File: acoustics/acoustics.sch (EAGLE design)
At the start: 174 parts

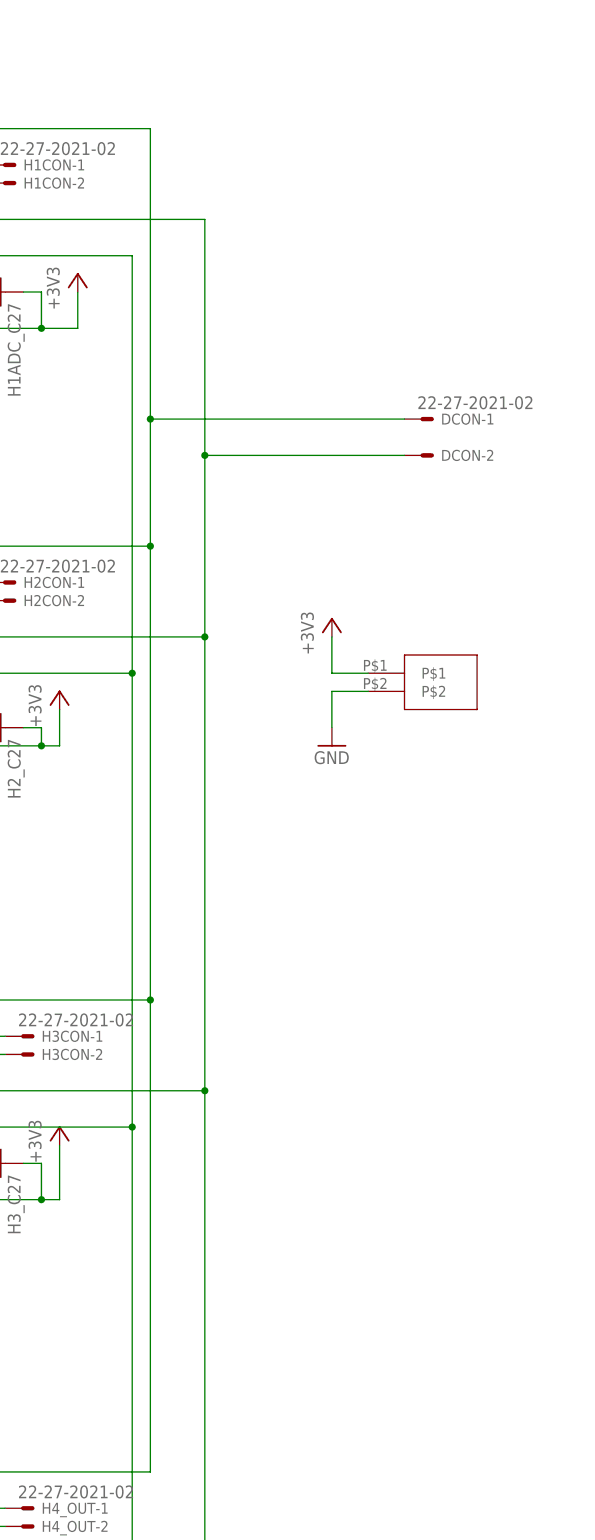
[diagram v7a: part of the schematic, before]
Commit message: Adding connectors and labels
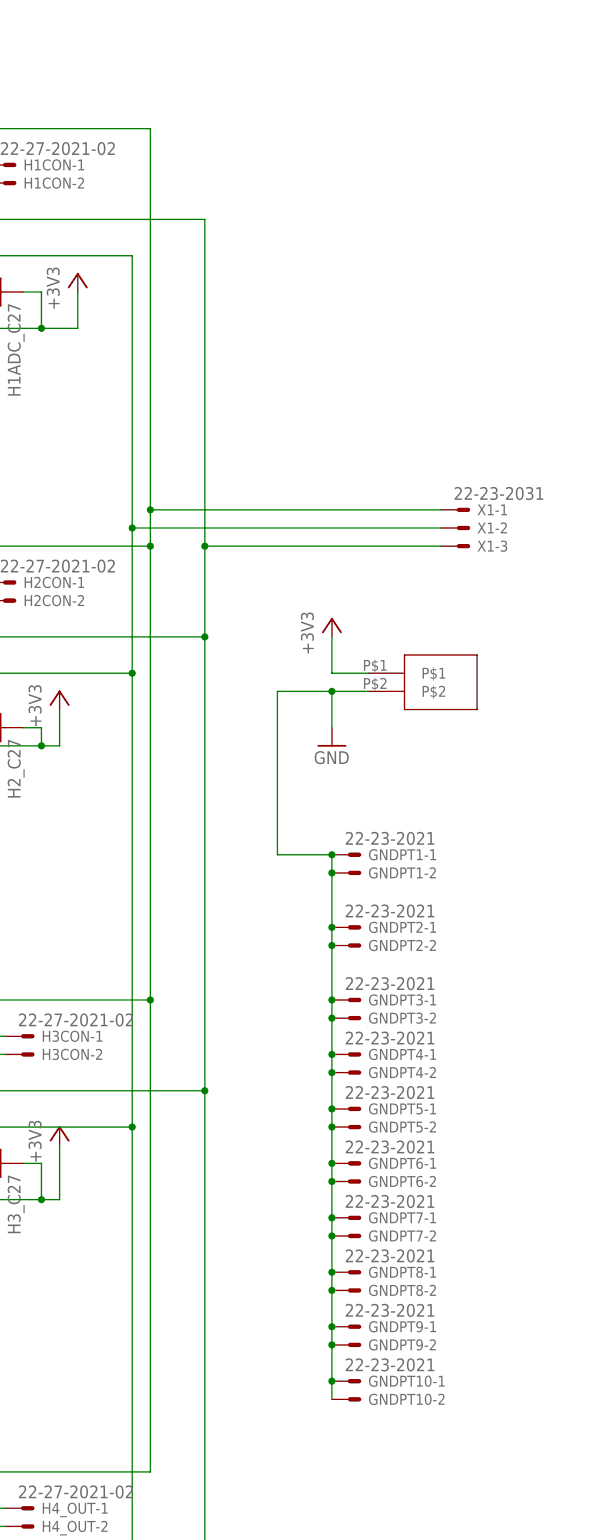
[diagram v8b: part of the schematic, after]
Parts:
- removed DCON: 22-27-2021-02, con-molex:22-27-2021-02
- added GNDPT1, GNDPT10, GNDPT2, GNDPT3, GNDPT4, GNDPT5, GNDPT6, GNDPT7, GNDPT8, GNDPT9: 22-23-2021, con-molex:22-23-2021
- added X1: 22-23-2031, con-molex:22-23-2031
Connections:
- net CLK: now also X1-2.S
- net GND: now also GNDPT1-1.S, GNDPT1-2.S, GNDPT10-1.S, GNDPT10-2.S, GNDPT2-1.S, GNDPT2-2.S, GNDPT3-1.S, GNDPT3-2.S, GNDPT4-1.S, GNDPT4-2.S, GNDPT5-1.S, GNDPT5-2.S, GNDPT6-1.S, GNDPT6-2.S, GNDPT7-1.S, GNDPT7-2.S, GNDPT8-1.S, GNDPT8-2.S, GNDPT9-1.S, GNDPT9-2.S
- net SCLK: now also X1-3.S; no longer DCON-2.S
- net START: now also X1-1.S; no longer DCON-1.S
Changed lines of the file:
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@@
 <part name="H3RF_C6" library="rcl" library_urn="urn:adsk.eagle:library:334" deviceset="C-EU" device="C0603" package3d_urn="urn:adsk.eagle:package:23616/2" value="47uf"/>
 <part name="H4_DIFAMP" library="THS4551" deviceset="THS4551" device=""/>
-<part name="DCON" library="con-molex" library_urn="urn:adsk.eagle:library:165" deviceset="22-?-02" device="27-2021"/>
 <part name="+3V21" library="supply1" library_urn="urn:adsk.eagle:library:371" deviceset="+3V3" device=""/>
 <part name="GND5" library="supply1" library_urn="urn:adsk.eagle:library:371" deviceset="GND" device=""/>
 <part name="U$2" library="105313-1102" deviceset="105313-1102" device=""/>
+<part name="X1" library="con-molex" library_urn="urn:adsk.eagle:library:165" deviceset="22-23-2031" device=""/>
+<part name="GNDPT1" library="con-molex" library_urn="urn:adsk.eagle:library:165" deviceset="22-23-2021" device=""/>
+<part name="GNDPT2" library="con-molex" library_urn="urn:adsk.eagle:library:165" deviceset="22-23-2021" device=""/>
+<part name="GNDPT3" library="con-molex" library_urn="urn:adsk.eagle:library:165" deviceset="22-23-2021" device=""/>
+<part name="GNDPT4" library="con-molex" library_urn="urn:adsk.eagle:library:165" deviceset="22-23-2021" device=""/>
+<part name="GNDPT5" library="con-molex" library_urn="urn:adsk.eagle:library:165" deviceset="22-23-2021" device=""/>
+<part name="GNDPT6" library="con-molex" library_urn="urn:adsk.eagle:library:165" deviceset="22-23-2021" device=""/>
+<part name="GNDPT7" library="con-molex" library_urn="urn:adsk.eagle:library:165" deviceset="22-23-2021" device=""/>
+<part name="GNDPT8" library="con-molex" library_urn="urn:adsk.eagle:library:165" deviceset="22-23-2021" device=""/>
+<part name="GNDPT9" library="con-molex" library_urn="urn:adsk.eagle:library:165" deviceset="22-23-2021" device=""/>
+<part name="GNDPT10" library="con-molex" library_urn="urn:adsk.eagle:library:165" deviceset="22-23-2021" device=""/>
 </parts>
 <sheets>
@@
 <instance part="H3RF_C6" gate="G$1" x="144.78" y="-73.66" rot="R180"/>
 <instance part="H4_DIFAMP" gate="G$1" x="30.48" y="-119.38"/>
-<instance part="DCON" gate="-1" x="337.82" y="33.02"/>
-<instance part="DCON" gate="-2" x="337.82" y="27.94"/>
 <instance part="+3V21" gate="G$1" x="325.12" y="5.08"/>
 <instance part="GND5" gate="1" x="325.12" y="-12.7"/>
 <instance part="U$2" gate="G$1" x="335.28" y="-5.08"/>
+<instance part="X1" gate="-1" x="342.9" y="20.32"/>
+<instance part="X1" gate="-2" x="342.9" y="17.78"/>
+<instance part="X1" gate="-3" x="342.9" y="15.24"/>
+<instance part="GNDPT1" gate="-1" x="327.66" y="-27.94"/>
+<instance part="GNDPT1" gate="-2" x="327.66" y="-30.48"/>
+<instance part="GNDPT2" gate="-1" x="327.66" y="-38.1"/>
+<instance part="GNDPT2" gate="-2" x="327.66" y="-40.64"/>
+<instance part="GNDPT3" gate="-1" x="327.66" y="-48.26"/>
+<instance part="GNDPT3" gate="-2" x="327.66" y="-50.8"/>
+<instance part="GNDPT4" gate="-1" x="327.66" y="-55.88"/>
+<instance part="GNDPT4" gate="-2" x="327.66" y="-58.42"/>
+<instance part="GNDPT5" gate="-1" x="327.66" y="-63.5"/>
+<instance part="GNDPT5" gate="-2" x="327.66" y="-66.04"/>
+<instance part="GNDPT6" gate="-1" x="327.66" y="-71.12"/>
+<instance part="GNDPT6" gate="-2" x="327.66" y="-73.66"/>
+<instance part="GNDPT7" gate="-1" x="327.66" y="-78.74"/>
+<instance part="GNDPT7" gate="-2" x="327.66" y="-81.28"/>
+<instance part="GNDPT8" gate="-1" x="327.66" y="-86.36"/>
+<instance part="GNDPT8" gate="-2" x="327.66" y="-88.9"/>
+<instance part="GNDPT9" gate="-1" x="327.66" y="-93.98"/>
+<instance part="GNDPT9" gate="-2" x="327.66" y="-96.52"/>
+<instance part="GNDPT10" gate="-1" x="327.66" y="-101.6"/>
+<instance part="GNDPT10" gate="-2" x="327.66" y="-104.14"/>
 </instances>
 <busses>
@@
 <pinref part="ADC_H1" gate="G$1" pin="START"/>
 <wire x1="236.22" y1="73.66" x2="299.72" y2="73.66" width="0.1524" layer="91"/>
-<wire x1="299.72" y1="73.66" x2="299.72" y2="33.02" width="0.1524" layer="91"/>
+<wire x1="299.72" y1="73.66" x2="299.72" y2="20.32" width="0.1524" layer="91"/>
 <junction x="299.72" y="15.24"/>
-<pinref part="DCON" gate="-1" pin="S"/>
-<wire x1="299.72" y1="33.02" x2="299.72" y2="15.24" width="0.1524" layer="91"/>
-<wire x1="335.28" y1="33.02" x2="299.72" y2="33.02" width="0.1524" layer="91"/>
-<junction x="299.72" y="33.02"/>
+<pinref part="X1" gate="-1" pin="S"/>
+<wire x1="299.72" y1="20.32" x2="299.72" y2="15.24" width="0.1524" layer="91"/>
+<wire x1="340.36" y1="20.32" x2="299.72" y2="20.32" width="0.1524" layer="91"/>
+<junction x="299.72" y="20.32"/>
 </segment>
 </net>
@@
 <wire x1="325.12" y1="-5.08" x2="325.12" y2="-10.16" width="0.1524" layer="91"/>
 <pinref part="U$2" gate="G$1" pin="P$2"/>
+<pinref part="GNDPT10" gate="-2" pin="S"/>
+<pinref part="GNDPT10" gate="-1" pin="S"/>
+<wire x1="325.12" y1="-104.14" x2="325.12" y2="-101.6" width="0.1524" layer="91"/>
+<pinref part="GNDPT9" gate="-2" pin="S"/>
+<wire x1="325.12" y1="-101.6" x2="325.12" y2="-96.52" width="0.1524" layer="91"/>
+<junction x="325.12" y="-101.6"/>
+<pinref part="GNDPT9" gate="-1" pin="S"/>
+<wire x1="325.12" y1="-96.52" x2="325.12" y2="-93.98" width="0.1524" layer="91"/>
+<junction x="325.12" y="-96.52"/>
+<pinref part="GNDPT8" gate="-2" pin="S"/>
+<wire x1="325.12" y1="-93.98" x2="325.12" y2="-88.9" width="0.1524" layer="91"/>
+<junction x="325.12" y="-93.98"/>
+<pinref part="GNDPT8" gate="-1" pin="S"/>
+<wire x1="325.12" y1="-88.9" x2="325.12" y2="-86.36" width="0.1524" layer="91"/>
+<junction x="325.12" y="-88.9"/>
+<pinref part="GNDPT7" gate="-2" pin="S"/>
+<wire x1="325.12" y1="-86.36" x2="325.12" y2="-81.28" width="0.1524" layer="91"/>
+<junction x="325.12" y="-86.36"/>
+<pinref part="GNDPT7" gate="-1" pin="S"/>
+<wire x1="325.12" y1="-81.28" x2="325.12" y2="-78.74" width="0.1524" layer="91"/>
+<junction x="325.12" y="-81.28"/>
+<pinref part="GNDPT6" gate="-2" pin="S"/>
+<wire x1="325.12" y1="-78.74" x2="325.12" y2="-73.66" width="0.1524" layer="91"/>
+<junction x="325.12" y="-78.74"/>
+<pinref part="GNDPT6" gate="-1" pin="S"/>
+<wire x1="325.12" y1="-73.66" x2="325.12" y2="-71.12" width="0.1524" layer="91"/>
+<junction x="325.12" y="-73.66"/>
+<pinref part="GNDPT5" gate="-2" pin="S"/>
+<wire x1="325.12" y1="-71.12" x2="325.12" y2="-66.04" width="0.1524" layer="91"/>
+<junction x="325.12" y="-71.12"/>
+<pinref part="GNDPT5" gate="-1" pin="S"/>
+<wire x1="325.12" y1="-66.04" x2="325.12" y2="-63.5" width="0.1524" layer="91"/>
+<junction x="325.12" y="-66.04"/>
+<pinref part="GNDPT4" gate="-2" pin="S"/>
+<wire x1="325.12" y1="-63.5" x2="325.12" y2="-58.42" width="0.1524" layer="91"/>
+<junction x="325.12" y="-63.5"/>
+<pinref part="GNDPT4" gate="-1" pin="S"/>
+<wire x1="325.12" y1="-58.42" x2="325.12" y2="-55.88" width="0.1524" layer="91"/>
+<junction x="325.12" y="-58.42"/>
+<pinref part="GNDPT3" gate="-2" pin="S"/>
+<wire x1="325.12" y1="-55.88" x2="325.12" y2="-50.8" width="0.1524" layer="91"/>
+<junction x="325.12" y="-55.88"/>
+<pinref part="GNDPT3" gate="-1" pin="S"/>
+<wire x1="325.12" y1="-50.8" x2="325.12" y2="-48.26" width="0.1524" layer="91"/>
+<junction x="325.12" y="-50.8"/>
+<pinref part="GNDPT2" gate="-2" pin="S"/>
+<wire x1="325.12" y1="-48.26" x2="325.12" y2="-40.64" width="0.1524" layer="91"/>
+<junction x="325.12" y="-48.26"/>
+<pinref part="GNDPT2" gate="-1" pin="S"/>
+<wire x1="325.12" y1="-40.64" x2="325.12" y2="-38.1" width="0.1524" layer="91"/>
+<junction x="325.12" y="-40.64"/>
+<pinref part="GNDPT1" gate="-2" pin="S"/>
+<wire x1="325.12" y1="-38.1" x2="325.12" y2="-30.48" width="0.1524" layer="91"/>
+<junction x="325.12" y="-38.1"/>
+<pinref part="GNDPT1" gate="-1" pin="S"/>
+<wire x1="325.12" y1="-30.48" x2="325.12" y2="-27.94" width="0.1524" layer="91"/>
+<junction x="325.12" y="-30.48"/>
+<wire x1="325.12" y1="-27.94" x2="317.5" y2="-27.94" width="0.1524" layer="91"/>
+<junction x="325.12" y="-27.94"/>
+<wire x1="317.5" y1="-27.94" x2="317.5" y2="-5.08" width="0.1524" layer="91"/>
+<wire x1="317.5" y1="-5.08" x2="325.12" y2="-5.08" width="0.1524" layer="91"/>
+<junction x="325.12" y="-5.08"/>
 </segment>
 </net>
@@
 <pinref part="ADC_H1" gate="G$1" pin="SCLK"/>
 <wire x1="236.22" y1="60.96" x2="307.34" y2="60.96" width="0.1524" layer="91"/>
-<wire x1="307.34" y1="60.96" x2="307.34" y2="27.94" width="0.1524" layer="91"/>
+<wire x1="307.34" y1="60.96" x2="307.34" y2="15.24" width="0.1524" layer="91"/>
 <junction x="307.34" y="2.54"/>
-<pinref part="DCON" gate="-2" pin="S"/>
-<wire x1="307.34" y1="27.94" x2="307.34" y2="2.54" width="0.1524" layer="91"/>
-<wire x1="335.28" y1="27.94" x2="307.34" y2="27.94" width="0.1524" layer="91"/>
-<junction x="307.34" y="27.94"/>
+<pinref part="X1" gate="-3" pin="S"/>
+<wire x1="307.34" y1="15.24" x2="307.34" y2="2.54" width="0.1524" layer="91"/>
+<wire x1="340.36" y1="15.24" x2="307.34" y2="15.24" width="0.1524" layer="91"/>
+<junction x="307.34" y="15.24"/>
 </segment>
 </net>
@@
 <wire x1="236.22" y1="55.88" x2="297.18" y2="55.88" width="0.1524" layer="91"/>
 <pinref part="ADC_H2" gate="G$1" pin="CLK"/>
-<wire x1="297.18" y1="55.88" x2="297.18" y2="-2.54" width="0.1524" layer="91"/>
+<wire x1="297.18" y1="55.88" x2="297.18" y2="17.78" width="0.1524" layer="91"/>
+<wire x1="297.18" y1="17.78" x2="297.18" y2="-2.54" width="0.1524" layer="91"/>
 <wire x1="297.18" y1="-2.54" x2="236.22" y2="-2.54" width="0.1524" layer="91"/>
 <pinref part="ADC_H3" gate="G$1" pin="CLK"/>
@@
 <wire x1="297.18" y1="-132.08" x2="236.22" y2="-132.08" width="0.1524" layer="91"/>
 <junction x="297.18" y="-66.04"/>
-</segment>
-</net>
+<pinref part="X1" gate="-2" pin="S"/>
+<wire x1="340.36" y1="17.78" x2="297.18" y2="17.78" width="0.1524" layer="91"/>
+<junction x="297.18" y="17.78"/>
+</segment>
+</net>
